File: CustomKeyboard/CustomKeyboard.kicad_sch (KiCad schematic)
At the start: 175 parts, among them J1 629105136821, SW1 PEC11H-RotaryEncoderSwitch, U1 ATMEGA32U4-AUR

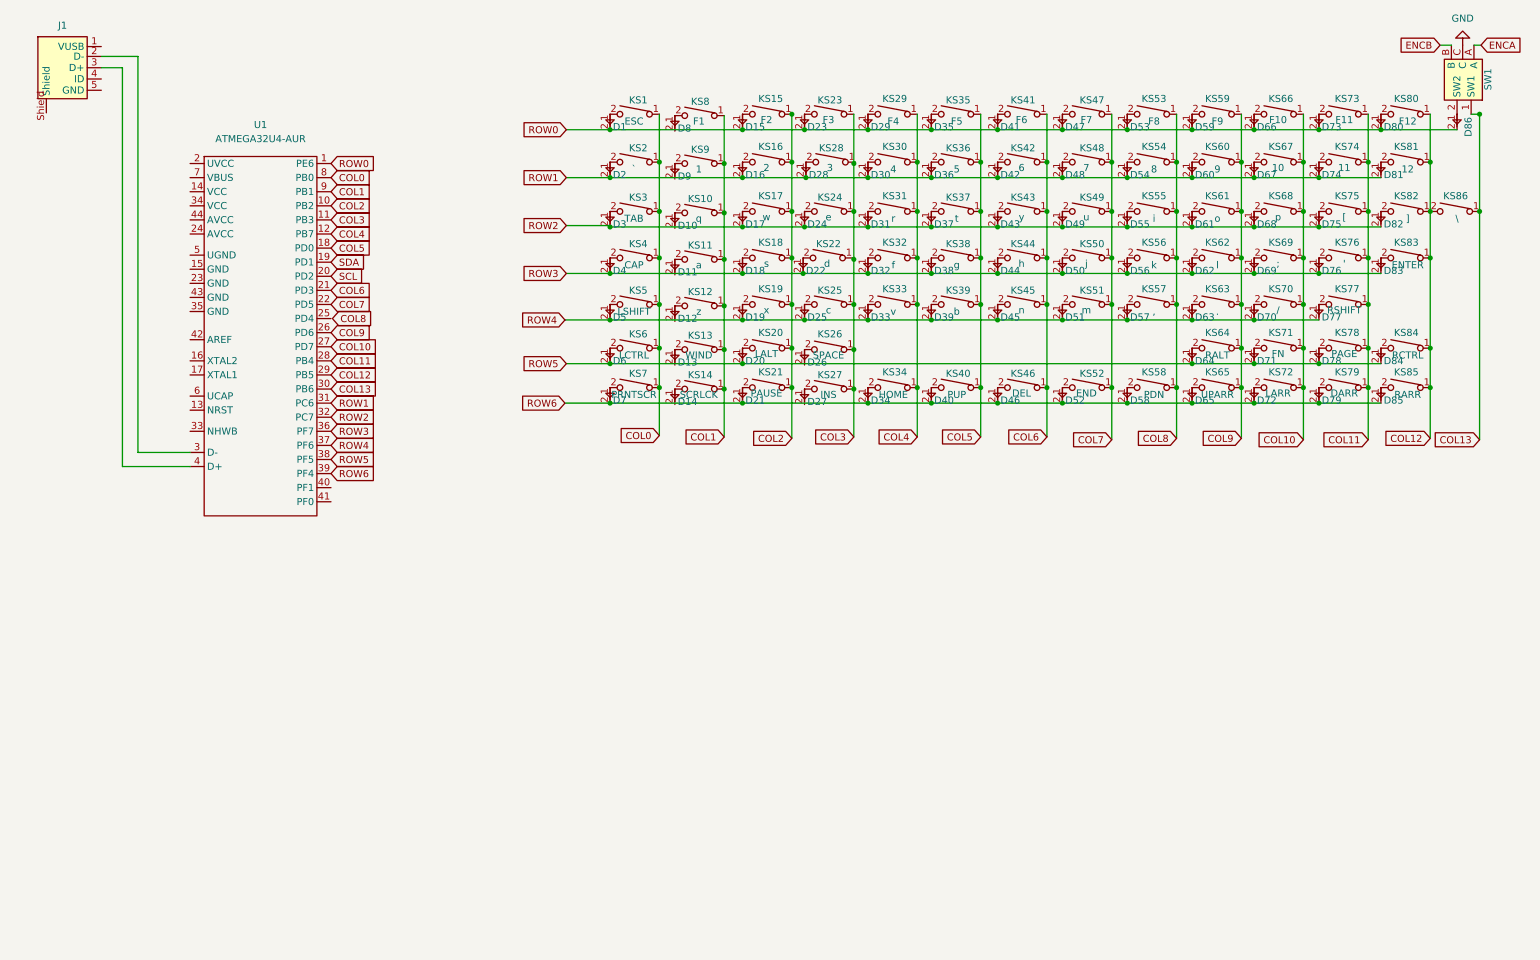
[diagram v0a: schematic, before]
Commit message: Finished Initial Footprints and started layout
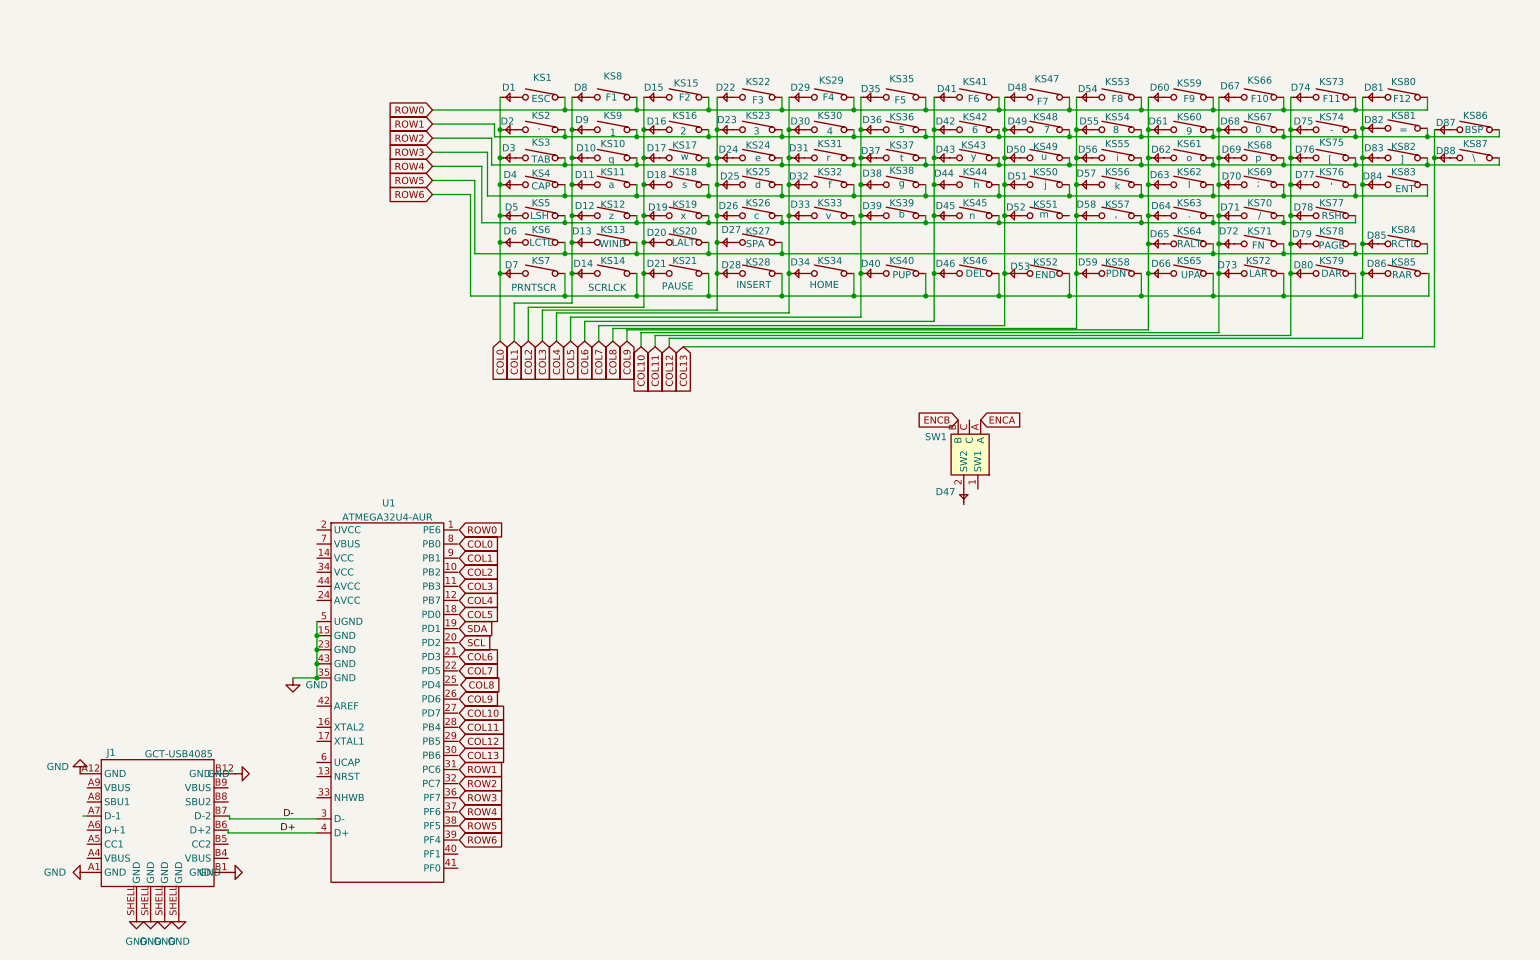
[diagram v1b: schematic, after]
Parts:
- removed D86: 1N4148WX-TP, keyboard_fp:SOD323, symbol symbols:1N4148WX-TP
- removed J1: 629105136821, keyboard_fp:629105136821(Wurth USB-BMicro), symbol symbols:629105136821
- added D47, D87, D88: 1N4148WX-TP, keyboard_fp:SOD323, symbol symbols:1N4148WX-TP
- added J1: GCT-USB4085, keyboard_fp:USB4085-GF-A, symbol symbols:GCT-USB4085
- added KS86: BSP, keyboard_fp:CherryMx, symbol symbols:KeyboardSwitch
- KS27: renamed from KS26; value SPACE -> SPA
- KS28: renamed from KS27; value INS -> INSERT
- KS5: value LSHIFT -> LSH
- KS6: value LCTRL -> LCTL
- KS65: value UPARR -> UPA
- KS67: value 10 -> 0
- KS72: value LARR -> LAR
- KS74: value 11 -> -
- KS77: value RSHIFT -> RSH
- KS79: value DARR -> DAR
- KS81: value 12 -> =
- KS83: value ENTER -> ENT
- KS84: value RCTRL -> RCTL
- KS85: value RARR -> RAR
- renumbered D23 to D22, D28 to D23, D22 to D25, D25 to D26, D26 to D27, D27 to D28, D47 to D48, D48 to D49, D49 to D50, D50 to D51, D51 to D52, D52 to D53, D53 to D54, D54 to D55, D55 to D56, D56 to D57, D57 to D58, D58 to D59, D59 to D60, D60 to D61, D61 to D62, D62 to D63, D63 to D64, D64 to D65, D65 to D66, D66 to D67, D67 to D68, D68 to D69, D69 to D70, D70 to D71, D71 to D72, D72 to D73, D73 to D74, D74 to D75, D75 to D76, D76 to D77, D77 to D78, D78 to D79, D79 to D80, D80 to D81, D81 to D82, D82 to D83, D83 to D84, D84 to D85, D85 to D86, KS23 to KS22, KS28 to KS23, KS22 to KS25, KS25 to KS26, KS86 to KS87
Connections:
- net COL0: now also D1.2, D2.2, D3.2, D4.2, D5.2, D6.2, D7.2; no longer KS1.1, KS2.1, KS3.1, KS4.1, KS5.1, KS6.1, KS7.1, U1.8 (PB0)
- net COL1: now also D10.2, D11.2, D12.2, D13.2, D14.2, D8.2, D9.2; no longer KS10.1, KS11.1, KS12.1, KS13.1, KS14.1, KS8.1, KS9.1, U1.9 (PB1)
- net COL10: now also D67.2, D68.2, D69.2, D70.2, D71.2, D72.2, D73.2; no longer KS66.1, KS67.1, KS68.1, KS69.1, KS70.1, KS71.1, KS72.1, U1.27 (PD7)
- net COL11: now also D74.2, D75.2, D76.2, D77.2, D78.2, D79.2, D80.2; no longer KS73.1, KS74.1, KS75.1, KS76.1, KS77.1, KS78.1, KS79.1, U1.28 (PB4)
- net COL12: now also D81.2, D82.2, D83.2, D84.2, D85.2, D86.2; no longer KS80.1, KS81.1, KS82.1, KS83.1, KS84.1, KS85.1, KS87.2, U1.29 (PB5)
- net COL13: now also D87.2, D88.2; no longer KS87.1, SW1.1 (SW1), U1.30 (PB6)
- net COL2: now also D15.2, D16.2, D17.2, D18.2, D19.2, D20.2, D21.2; no longer KS15.1, KS16.1, KS17.1, KS18.1, KS19.1, KS20.1, KS21.1, U1.10 (PB2)
- net COL3: now also D22.2, D23.2, D24.2, D25.2, D26.2, D27.2, D28.2; no longer KS22.1, KS23.1, KS24.1, KS25.1, KS26.1, KS27.1, KS28.1, U1.11 (PB3)
- net COL4: now also D29.2, D30.2, D31.2, D32.2, D33.2, D34.2; no longer KS29.1, KS30.1, KS31.1, KS32.1, KS33.1, KS34.1, U1.12 (PB7)
- net COL5: now also D35.2, D36.2, D37.2, D38.2, D39.2, D40.2; no longer KS35.1, KS36.1, KS37.1, KS38.1, KS39.1, KS40.1, U1.18 (PD0)
- net COL6: now also D41.2, D42.2, D43.2, D44.2, D45.2, D46.2; no longer KS41.1, KS42.1, KS43.1, KS44.1, KS45.1, KS46.1, U1.21 (PD3)
- net COL7: now also D48.2, D49.2, D50.2, D51.2, D52.2, D53.2; no longer KS47.1, KS48.1, KS49.1, KS50.1, KS51.1, KS52.1, U1.22 (PD5)
- net COL8: now also D54.2, D55.2, D56.2, D57.2, D58.2, D59.2; no longer KS53.1, KS54.1, KS55.1, KS56.1, KS57.1, KS58.1
- net COL9: now also D60.2, D61.2, D62.2, D63.2, D64.2, D65.2, D66.2; no longer KS59.1, KS60.1, KS61.1, KS62.1, KS63.1, KS64.1, KS65.1, U1.26 (PD6)
- net GND: now also U1.15 (GND), U1.23 (GND), U1.35 (GND), U1.43 (GND), U1.5 (UGND), J1.A1 (GND), J1.A12 (GND), J1.B1 (GND), J1.B12 (GND), J1.SHELL (GND); no longer SW1.C
- net ROW0: now also KS1.1, KS15.1, KS22.1, KS29.1, KS35.1, KS41.1, KS47.1, KS53.1, KS59.1, KS66.1, KS73.1, KS8.1, KS80.1; no longer D1.2, D15.2, D22.2, D29.2, D35.2, D41.2, D48.2, D54.2, D60.2, D67.2, D74.2, D81.2, U1.1 (PE6)
- net ROW1: now also KS16.1, KS2.1, KS23.1, KS30.1, KS36.1, KS42.1, KS48.1, KS54.1, KS60.1, KS67.1, KS74.1, KS81.1, KS9.1, KS86.1; no longer D16.2, D2.2, D23.2, D30.2, D36.2, D42.2, D49.2, D55.2, D61.2, D68.2, D75.2, D82.2, U1.31 (PC6)
- net ROW2: now also KS10.1, KS17.1, KS24.1, KS3.1, KS31.1, KS37.1, KS43.1, KS49.1, KS55.1, KS61.1, KS68.1, KS75.1, KS82.1, KS87.1; no longer D17.2, D24.2, D3.2, D31.2, D37.2, D43.2, D50.2, D56.2, D62.2, D69.2, D76.2, D83.2, U1.32 (PC7)
- net ROW3: now also KS11.1, KS18.1, KS25.1, KS32.1, KS38.1, KS4.1, KS44.1, KS50.1, KS56.1, KS62.1, KS69.1, KS76.1, KS83.1; no longer D18.2, D25.2, D32.2, D38.2, D4.2, D44.2, D51.2, D57.2, D63.2, D70.2, D77.2, D84.2, U1.36 (PF7)
- net ROW4: now also KS12.1, KS19.1, KS26.1, KS33.1, KS39.1, KS45.1, KS5.1, KS57.1, KS63.1, KS70.1, KS77.1; no longer D19.2, D26.2, D33.2, D39.2, D45.2, D5.2, D52.2, D58.2, D64.2, D71.2, D78.2, U1.37 (PF6)
- net ROW5: now also KS13.1, KS20.1, KS27.1, KS6.1, KS64.1, KS71.1, KS78.1, KS84.1; no longer D20.2, D6.2, D65.2, D72.2, D79.2, D85.2, U1.38 (PF5)
- net ROW6: now also KS14.1, KS21.1, KS28.1, KS34.1, KS40.1, KS46.1, KS52.1, KS58.1, KS65.1, KS7.1, KS72.1, KS79.1, KS85.1; no longer D21.2, D34.2, D40.2, D46.2, D53.2, D59.2, D66.2, D7.2, D73.2, D80.2, D86.2, U1.39 (PF4)
- net SCL: no longer U1.20 (PD2)
- net SDA: no longer U1.19 (PD1)
- net at SW1.2 (SW2): now also D47.1
- net D-: now reaches U1.3 (D-)
- net D-: now also J1.B7 (D-2)
- net D+: now reaches U1.4 (D+)
- net D+: now also J1.B6 (D+2)
- new net: D87.1, KS86.2
- new net: D88.1, KS87.2
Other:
- moved on the sheet: U1

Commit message: stuff
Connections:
- net COL0: now also U1.8 (PB0)
- net COL1: now also U1.9 (PB1)
- net COL10: now also U1.27 (PD7)
- net COL11: now also U1.28 (PB4)
- net COL12: now also U1.29 (PB5)
- net COL13: now also U1.30 (PB6)
- net COL2: now also U1.10 (PB2)
- net COL3: now also U1.11 (PB3)
- net COL4: now also U1.12 (PB7)
- net COL5: now also U1.18 (PD0)
- net COL6: now also U1.21 (PD3)
- net COL7: now also U1.22 (PD5)
- net COL9: now also U1.26 (PD6)
- net D+: now also J1.A6 (D+1); no longer J1.B6 (D+2)
- net D-: now also J1.A7 (D-1); no longer J1.B7 (D-2)
- net ROW0: now also U1.1 (PE6)
- net ROW1: now also U1.31 (PC6)
- net ROW2: now also U1.32 (PC7)
- net ROW3: now also U1.36 (PF7)
- net ROW4: now also U1.37 (PF6)
- net ROW5: now also U1.38 (PF5)
- net ROW6: now also U1.39 (PF4)
- net SCL: now also U1.20 (PD2)
- net SDA: now also U1.19 (PD1)
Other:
- moved on the sheet: J1
